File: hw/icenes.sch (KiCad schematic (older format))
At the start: 72 parts, among them J1 USB_B_Micro, J2 Barrel_Jack_Switch, U1 TPS62050, U2 TPS62050, U3 TPS62056, U4 iCE40HX8K-CT256

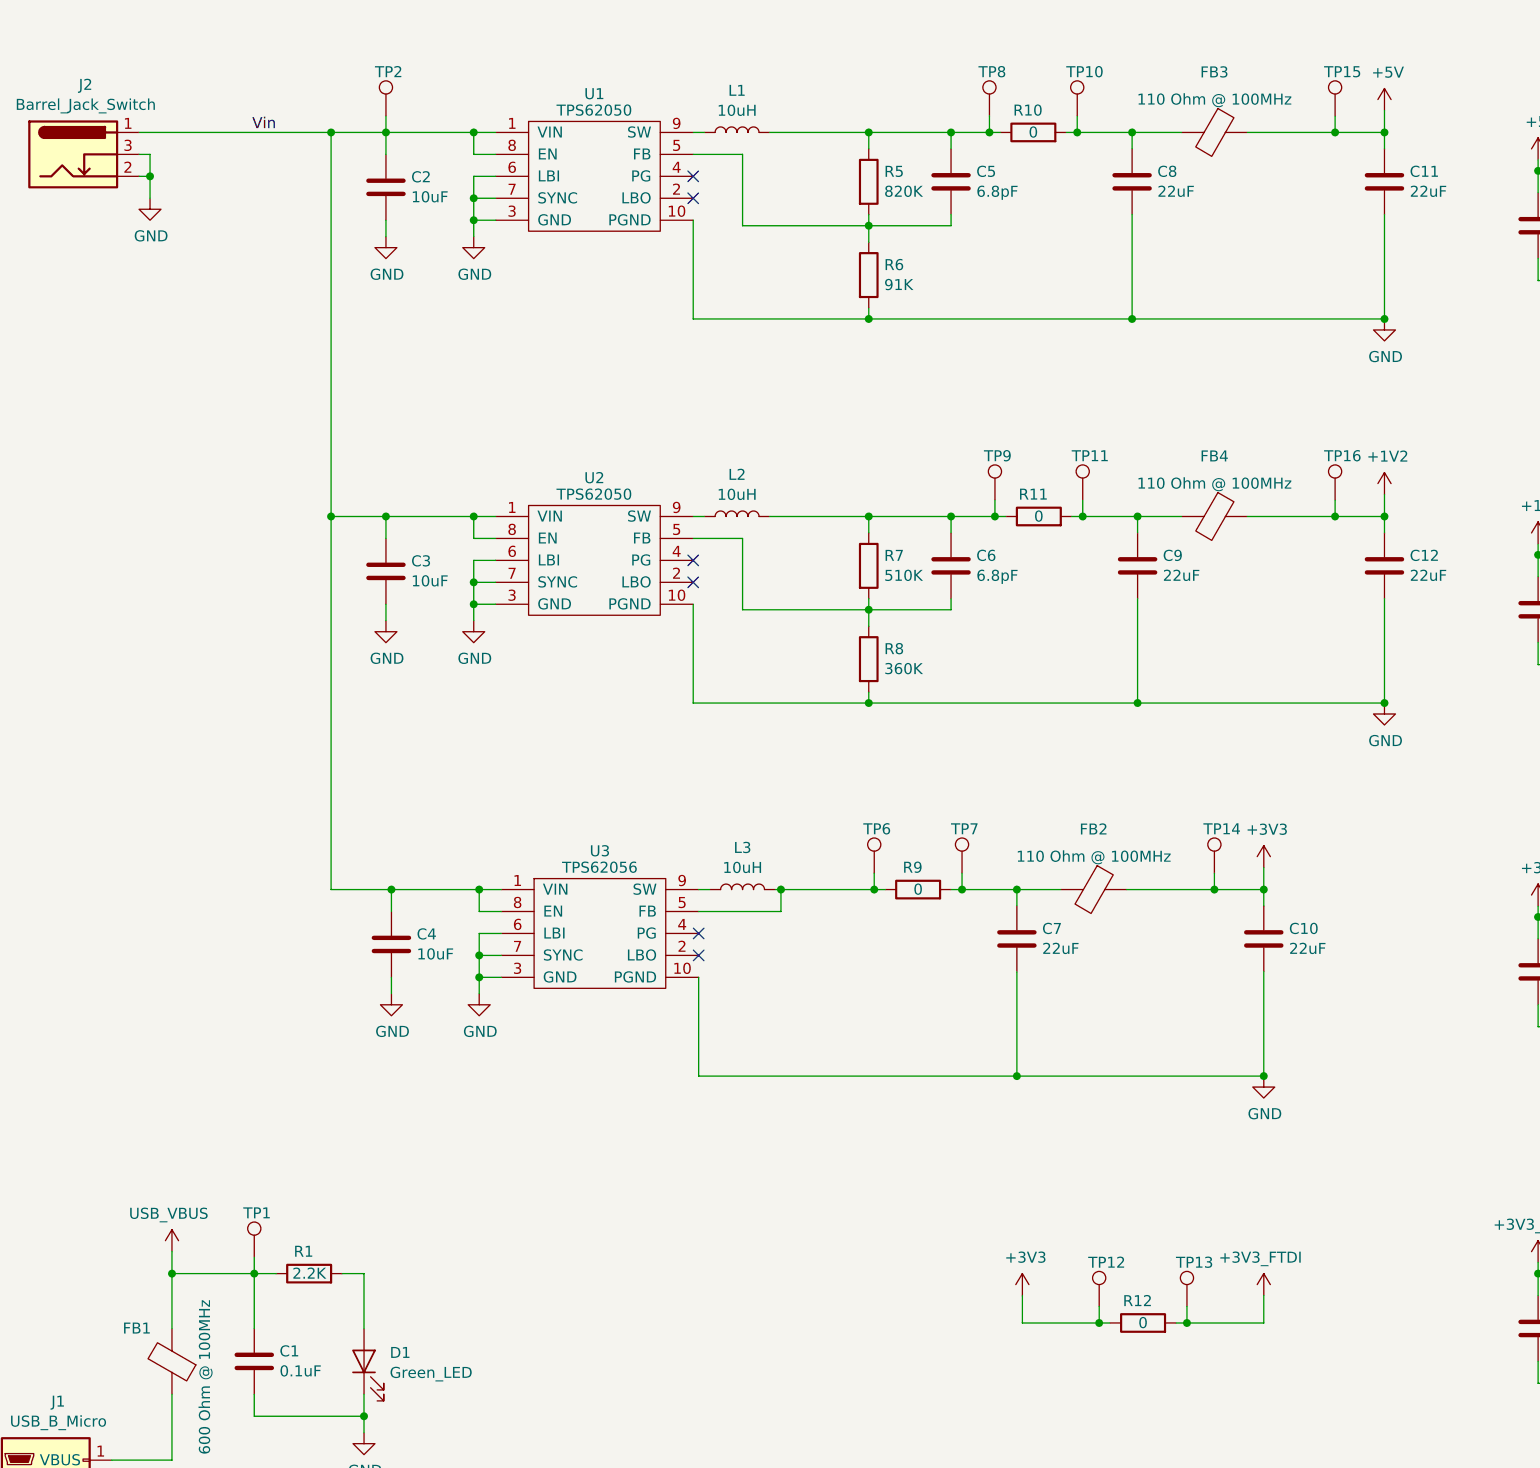
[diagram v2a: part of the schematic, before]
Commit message: Added voltage range in Vin lable (+5V to +10V).
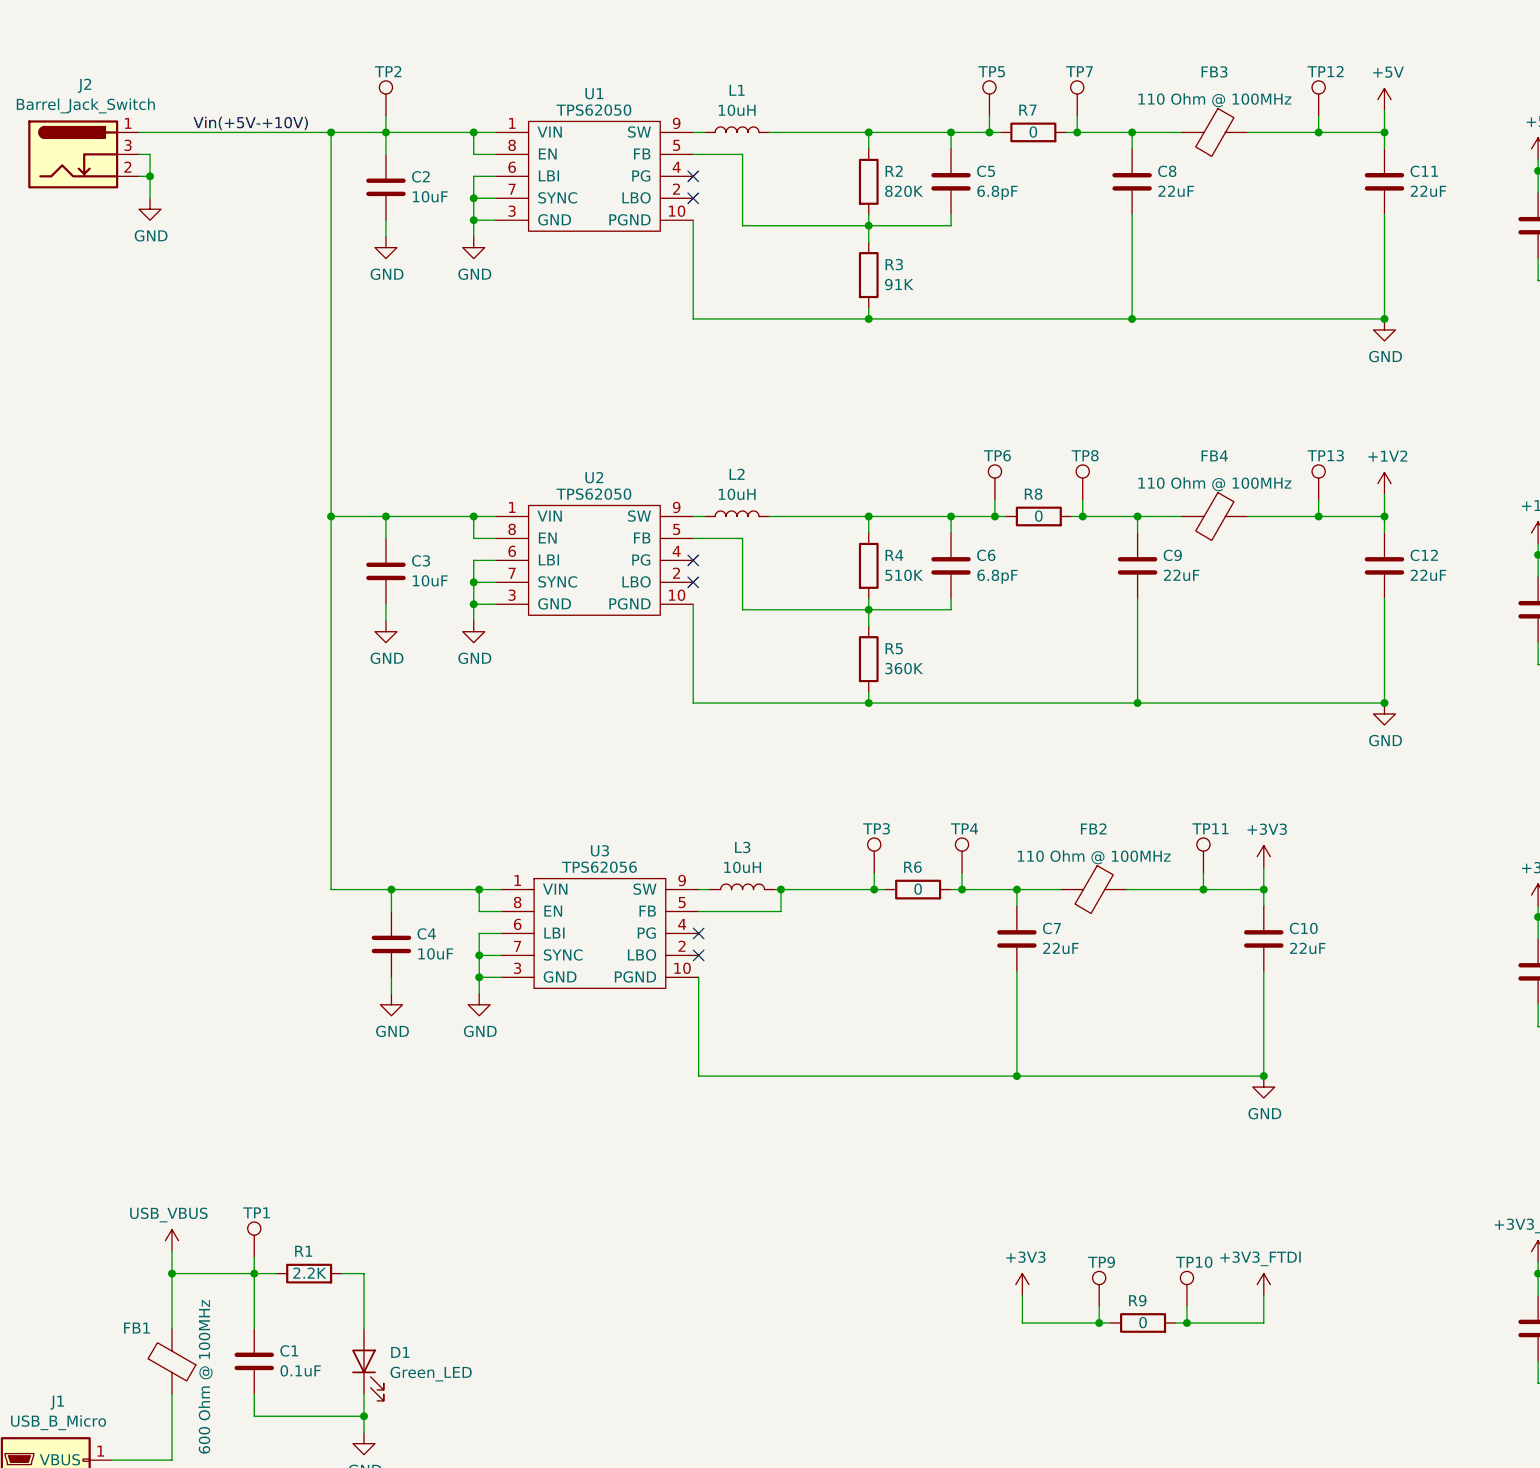
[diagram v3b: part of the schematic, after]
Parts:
- renumbered R5 to R2, R6 to R3, R7 to R4, R8 to R5, R9 to R6, R10 to R7, R11 to R8, R12 to R9, TP13 to TP10, TP14 to TP11, TP15 to TP12, TP16 to TP13, TP6 to TP3, TP7 to TP4, TP8 to TP5, TP9 to TP6, TP10 to TP7, TP11 to TP8, TP12 to TP9
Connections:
- net Vin renamed Vin(+5V-+10V)
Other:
- moved on the sheet: TP11, TP12, TP13
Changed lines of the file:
@@
 F1 "icenes-nes-connector.sch" 50
 $EndSheet
-Text Label 3000 1550 2    50   ~ 0
-Vin
+Text Label 3150 1550 2    50   ~ 0
+Vin(+5V-+10V)
 $Comp
 L power:+3V3 #PWR012
@@
 	6075 5000 6125 5000
 $Comp
-L icenes-library:R0 R9
+L icenes-library:R0 R6
 U 1 1 5D6A7F7F
 P 5925 5000
-F 0 "R9" H 5900 5100 50  0000 C CNN
+F 0 "R6" H 5900 5100 50  0000 C CNN
 F 1 "R0" H 5925 4900 50  0001 C CNN
 F 2 "Resistor_SMD:R_0805_2012Metric_Pad1.15x1.40mm_HandSolder" V 5925 5000 50  0001 C CNN
@@
 	6625 3300 6675 3300
 $Comp
-L icenes-library:R0 R11
+L icenes-library:R0 R8
 U 1 1 5D56A60B
 P 6475 3300
-F 0 "R11" H 6450 3400 50  0000 C CNN
+F 0 "R8" H 6450 3400 50  0000 C CNN
 F 1 "R0" H 6475 3200 50  0001 C CNN
 F 2 "Resistor_SMD:R_0805_2012Metric_Pad1.15x1.40mm_HandSolder" V 6475 3300 50  0001 C CNN
@@
 $EndComp
 $Comp
-L icenes-library:R360K R8
+L icenes-library:R360K R5
 U 1 1 5D43172D
 P 5700 3950
-F 0 "R8" V 5654 4020 50  0000 L CNN
+F 0 "R5" V 5654 4020 50  0000 L CNN
 F 1 "R360K" H 5700 3850 50  0001 C CNN
 F 2 "Resistor_SMD:R_0603_1608Metric_Pad1.05x0.95mm_HandSolder" V 5700 3950 50  0001 C CNN
@@
 $EndComp
 $Comp
-L icenes-library:R510K R7
+L icenes-library:R510K R4
 U 1 1 5D4301E7
 P 5700 3525
-F 0 "R7" V 5654 3595 50  0000 L CNN
+F 0 "R4" V 5654 3595 50  0000 L CNN
 F 1 "R510K" H 5700 3425 50  0001 C CNN
 F 2 "Resistor_SMD:R_0603_1608Metric_Pad1.05x0.95mm_HandSolder" V 5700 3525 50  0001 C CNN
@@
 $EndComp
 $Comp
-L icenes-library:R0 R10
+L icenes-library:R0 R7
 U 1 1 5D4F2DE1
 P 6450 1550
-F 0 "R10" H 6425 1650 50  0000 C CNN
+F 0 "R7" H 6425 1650 50  0000 C CNN
 F 1 "R0" H 6450 1450 50  0001 C CNN
 F 2 "Resistor_SMD:R_0805_2012Metric_Pad1.15x1.40mm_HandSolder" V 6450 1550 50  0001 C CNN
@@
 Connection ~ 6075 1550
 $Comp
-L icenes-library:R820K R5
+L icenes-library:R820K R2
 U 1 1 5D37D2E8
 P 5700 1775
-F 0 "R5" V 5654 1845 50  0000 L CNN
+F 0 "R2" V 5654 1845 50  0000 L CNN
 F 1 "R820K" H 5700 1675 50  0001 C CNN
 F 2 "Resistor_SMD:R_0603_1608Metric_Pad1.05x0.95mm_HandSolder" V 5700 1775 50  0001 C CNN
@@
 $EndComp
 $Comp
-L icenes-library:R91K R6
+L icenes-library:R91K R3
 U 1 1 5D37EA73
 P 5700 2200
-F 0 "R6" V 5654 2270 50  0000 L CNN
+F 0 "R3" V 5654 2270 50  0000 L CNN
 F 1 "R91K" H 5700 2100 50  0001 C CNN
 F 2 "Resistor_SMD:R_0603_1608Metric_Pad1.05x0.95mm_HandSolder" V 5700 2200 50  0001 C CNN
@@
 $EndComp
 $Comp
-L icenes-library:TestPoint TP8
+L icenes-library:TestPoint TP5
 U 1 1 5D7111E6
 P 6250 1475
-F 0 "TP8" H 6200 1675 50  0000 L CNN
+F 0 "TP5" H 6200 1675 50  0000 L CNN
 F 1 "TestPoint" H 6250 1675 50  0001 C CNN
 F 2 "TestPoint:TestPoint_Pad_D1.0mm" H 6450 1475 50  0001 C CNN
@@
 $EndComp
 $Comp
-L icenes-library:TestPoint TP10
+L icenes-library:TestPoint TP7
 U 1 1 5D712B7B
 P 6650 1475
-F 0 "TP10" H 6600 1675 50  0000 L CNN
+F 0 "TP7" H 6600 1675 50  0000 L CNN
 F 1 "TestPoint" H 6650 1675 50  0001 C CNN
 F 2 "TestPoint:TestPoint_Pad_D1.0mm" H 6850 1475 50  0001 C CNN
@@
 $EndComp
 $Comp
-L icenes-library:TestPoint TP9
+L icenes-library:TestPoint TP6
 U 1 1 5D724BBE
 P 6275 3225
-F 0 "TP9" H 6225 3425 50  0000 L CNN
+F 0 "TP6" H 6225 3425 50  0000 L CNN
 F 1 "TestPoint" H 6275 3425 50  0001 C CNN
 F 2 "TestPoint:TestPoint_Pad_D1.0mm" H 6475 3225 50  0001 C CNN
@@
 $EndComp
 $Comp
-L icenes-library:TestPoint TP11
+L icenes-library:TestPoint TP8
 U 1 1 5D735BB7
 P 6675 3225
-F 0 "TP11" H 6625 3425 50  0000 L CNN
+F 0 "TP8" H 6625 3425 50  0000 L CNN
 F 1 "TestPoint" H 6675 3425 50  0001 C CNN
 F 2 "TestPoint:TestPoint_Pad_D1.0mm" H 6875 3225 50  0001 C CNN
@@
 $EndComp
 $Comp
-L icenes-library:TestPoint TP6
+L icenes-library:TestPoint TP3
 U 1 1 5D746D9B
 P 5725 4925
-F 0 "TP6" H 5675 5125 50  0000 L CNN
+F 0 "TP3" H 5675 5125 50  0000 L CNN
 F 1 "TestPoint" H 5725 5125 50  0001 C CNN
 F 2 "TestPoint:TestPoint_Pad_D1.0mm" H 5925 4925 50  0001 C CNN
@@
 $EndComp
 $Comp
-L icenes-library:TestPoint TP7
+L icenes-library:TestPoint TP4
 U 1 1 5D758010
 P 6125 4925
-F 0 "TP7" H 6075 5125 50  0000 L CNN
+F 0 "TP4" H 6075 5125 50  0000 L CNN
 F 1 "TestPoint" H 6125 5125 50  0001 C CNN
 F 2 "TestPoint:TestPoint_Pad_D1.0mm" H 6325 4925 50  0001 C CNN
@@
 Connection ~ 8050 1550
 Connection ~ 8050 2400
-Wire Wire Line
-	7825 1475 7825 1550
-$Comp
-L icenes-library:TestPoint TP15
+$Comp
+L icenes-library:TestPoint TP12
 U 1 1 5D69F2EA
-P 7825 1475
-F 0 "TP15" H 7775 1675 50  0000 L CNN
-F 1 "TestPoint" H 7825 1675 50  0001 C CNN
-F 2 "TestPoint:TestPoint_Pad_D1.0mm" H 8025 1475 50  0001 C CNN
-F 3 "~" H 8025 1475 50  0001 C CNN
-	1    7825 1475
-	1    0    0    -1
-$EndComp
-Connection ~ 7825 1550
+P 7750 1475
+F 0 "TP12" H 7700 1675 50  0000 L CNN
+F 1 "TestPoint" H 7750 1675 50  0001 C CNN
+F 2 "TestPoint:TestPoint_Pad_D1.0mm" H 7950 1475 50  0001 C CNN
+F 3 "~" H 7950 1475 50  0001 C CNN
+	1    7750 1475
+	1    0    0    -1
+$EndComp
 Wire Wire Line
 	6900 2400 8050 2400
@@
 	8050 3300 8050 3375
 Connection ~ 8050 3300
-Wire Wire Line
-	7825 3225 7825 3300
-$Comp
-L icenes-library:TestPoint TP16
+$Comp
+L icenes-library:TestPoint TP13
 U 1 1 5D7086C1
-P 7825 3225
-F 0 "TP16" H 7775 3425 50  0000 L CNN
-F 1 "TestPoint" H 7825 3425 50  0001 C CNN
-F 2 "TestPoint:TestPoint_Pad_D1.0mm" H 8025 3225 50  0001 C CNN
-F 3 "~" H 8025 3225 50  0001 C CNN
-	1    7825 3225
-	1    0    0    -1
-$EndComp
-Connection ~ 7825 3300
+P 7750 3225
+F 0 "TP13" H 7700 3425 50  0000 L CNN
+F 1 "TestPoint" H 7750 3425 50  0001 C CNN
+F 2 "TestPoint:TestPoint_Pad_D1.0mm" H 7950 3225 50  0001 C CNN
+F 3 "~" H 7950 3225 50  0001 C CNN
+	1    7750 3225
+	1    0    0    -1
+$EndComp
 Wire Wire Line
 	5700 4150 6925 4150
@@
 	7500 5000 7500 5075
 Connection ~ 7500 5000
-Wire Wire Line
-	7275 4925 7275 5000
-$Comp
-L icenes-library:TestPoint TP14
+$Comp
+L icenes-library:TestPoint TP11
 U 1 1 5D7AD8D4
-P 7275 4925
-F 0 "TP14" H 7225 5125 50  0000 L CNN
-F 1 "TestPoint" H 7275 5125 50  0001 C CNN
-F 2 "TestPoint:TestPoint_Pad_D1.0mm" H 7475 4925 50  0001 C CNN
-F 3 "~" H 7475 4925 50  0001 C CNN
-	1    7275 4925
-	1    0    0    -1
-$EndComp
-Connection ~ 7275 5000
+P 7225 4925
+F 0 "TP11" H 7175 5125 50  0000 L CNN
+F 1 "TestPoint" H 7225 5125 50  0001 C CNN
+F 2 "TestPoint:TestPoint_Pad_D1.0mm" H 7425 4925 50  0001 C CNN
+F 3 "~" H 7425 4925 50  0001 C CNN
+	1    7225 4925
+	1    0    0    -1
+$EndComp
 Wire Wire Line
 	6375 5850 7500 5850
 Connection ~ 7500 5850
 Wire Wire Line
-	7425 1550 7825 1550
-Wire Wire Line
 	7125 1550 6900 1550
 Connection ~ 6900 1550
 Wire Wire Line
-	7425 3300 7825 3300
-Wire Wire Line
 	7125 3300 6925 3300
 Connection ~ 6925 3300
-Wire Wire Line
-	6875 5000 7275 5000
 Wire Wire Line
 	6575 5000 6375 5000
@@
 Wire Wire Line
 	14300 7250 14100 7250
-Wire Wire Line
-	7275 5000 7500 5000
-Wire Wire Line
-	7825 3300 8050 3300
-Wire Wire Line
-	7825 1550 8050 1550
 $Comp
 L power:GND #PWR024
@@
 	7100 6975 7150 6975
 $Comp
-L icenes-library:R0 R12
+L icenes-library:R0 R9
 U 1 1 5DBD6898
 P 6950 6975
-AR Path="/5DBD6898" Ref="R12"  Part="1"
+AR Path="/5DBD6898" Ref="R9"  Part="1"
 AR Path="/5D1BAC88/5DBD6898" Ref="R?"  Part="1"
-F 0 "R12" H 6925 7075 50  0000 C CNN
+F 0 "R9" H 6925 7075 50  0000 C CNN
 F 1 "R0" H 6950 6875 50  0001 C CNN
 F 2 "Resistor_SMD:R_0805_2012Metric_Pad1.15x1.40mm_HandSolder" V 6950 6975 50  0001 C CNN
@@
 	6400 6975 6750 6975
 $Comp
-L icenes-library:TestPoint TP12
+L icenes-library:TestPoint TP9
 U 1 1 5DBD68AA
 P 6750 6900
-AR Path="/5DBD68AA" Ref="TP12"  Part="1"
+AR Path="/5DBD68AA" Ref="TP9"  Part="1"
 AR Path="/5D1BAC88/5DBD68AA" Ref="TP?"  Part="1"
-F 0 "TP12" H 6700 7100 50  0000 L CNN
+F 0 "TP9" H 6700 7100 50  0000 L CNN
 F 1 "TestPoint" H 6750 7100 50  0001 C CNN
 F 2 "TestPoint:TestPoint_Pad_D1.0mm" H 6950 6900 50  0001 C CNN
@@
 $EndComp
 $Comp
-L icenes-library:TestPoint TP13
+L icenes-library:TestPoint TP10
 U 1 1 5DBD68B0
 P 7150 6900
-AR Path="/5DBD68B0" Ref="TP13"  Part="1"
+AR Path="/5DBD68B0" Ref="TP10"  Part="1"
 AR Path="/5D1BAC88/5DBD68B0" Ref="TP?"  Part="1"
-F 0 "TP13" H 7100 7100 50  0000 L CNN
+F 0 "TP10" H 7100 7100 50  0000 L CNN
 F 1 "TestPoint" H 7150 7100 50  0001 C CNN
 F 2 "TestPoint:TestPoint_Pad_D1.0mm" H 7350 6900 50  0001 C CNN
@@
 	5300 5000 5725 5000
 NoConn ~ 4925 5200
+Wire Wire Line
+	7425 1550 7750 1550
+Wire Wire Line
+	7750 1475 7750 1550
+Connection ~ 7750 1550
+Wire Wire Line
+	7750 1550 8050 1550
+Wire Wire Line
+	7425 3300 7750 3300
+Wire Wire Line
+	7750 3225 7750 3300
+Connection ~ 7750 3300
+Wire Wire Line
+	7750 3300 8050 3300
+Wire Wire Line
+	6875 5000 7225 5000
+Wire Wire Line
+	7225 4925 7225 5000
+Connection ~ 7225 5000
+Wire Wire Line
+	7225 5000 7500 5000
 $EndSCHEMATC

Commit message: Changed inductor.
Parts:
- L1, L2, L3: footprint Inductor_SMD:L_1812_4532Metric_Pad1.30x3.40mm_HandSolder -> icenes-library:Sumida_L_7.5x7.5_H4.5; Manufacturer Coilcraft -> Sumida; Part number 1812PS-103JLB -> CDRH74NP-100MC-B
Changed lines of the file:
@@
 F 0 "L3" V 5315 5000 50  0000 C CNN
 F 1 "L10uH" V 5200 5000 50  0001 C CNN
-F 2 "Inductor_SMD:L_1812_4532Metric_Pad1.30x3.40mm_HandSolder" H 5125 5000 50  0001 C CNN
-F 3 "https://www.mouser.se/datasheet/2/597/1812ps-270619.pdf" H 5125 5000 50  0001 C CNN
+F 2 "icenes-library:Sumida_L_7.5x7.5_H4.5" H 5125 5000 50  0001 C CNN
+F 3 "https://www.mouser.se/datasheet/2/390/CDRH74-514269.pdf" H 5125 5000 50  0001 C CNN
 F 4 "10uH" V 5224 5000 50  0000 C CNN "Inductance"
-F 5 "Coilcraft " H 5125 5000 50  0001 C CNN "Manufacturer"
-F 6 "1812PS-103JLB" H 5125 5000 50  0001 C CNN "Part number"
+F 5 "Sumida " H 5125 5000 50  0001 C CNN "Manufacturer"
+F 6 "CDRH74NP-100MC-B" H 5125 5000 50  0001 C CNN "Part number"
 	1    5125 5000
 	0    -1   -1   0
@@
 F 0 "L2" V 5290 3300 50  0000 C CNN
 F 1 "L10uH" V 5175 3300 50  0001 C CNN
-F 2 "Inductor_SMD:L_1812_4532Metric_Pad1.30x3.40mm_HandSolder" H 5100 3300 50  0001 C CNN
-F 3 "https://www.mouser.se/datasheet/2/597/1812ps-270619.pdf" H 5100 3300 50  0001 C CNN
+F 2 "icenes-library:Sumida_L_7.5x7.5_H4.5" H 5100 3300 50  0001 C CNN
+F 3 "https://www.mouser.se/datasheet/2/390/CDRH74-514269.pdf" H 5100 3300 50  0001 C CNN
 F 4 "10uH" V 5199 3300 50  0000 C CNN "Inductance"
-F 5 "Coilcraft " H 5100 3300 50  0001 C CNN "Manufacturer"
-F 6 "1812PS-103JLB" H 5100 3300 50  0001 C CNN "Part number"
+F 5 "Sumida " H 5100 3300 50  0001 C CNN "Manufacturer"
+F 6 "CDRH74NP-100MC-B" H 5100 3300 50  0001 C CNN "Part number"
 	1    5100 3300
 	0    -1   -1   0
@@
 F 0 "L1" V 5290 1550 50  0000 C CNN
 F 1 "L10uH" V 5175 1550 50  0001 C CNN
-F 2 "Inductor_SMD:L_1812_4532Metric_Pad1.30x3.40mm_HandSolder" H 5100 1550 50  0001 C CNN
-F 3 "https://www.mouser.se/datasheet/2/597/1812ps-270619.pdf" H 5100 1550 50  0001 C CNN
+F 2 "icenes-library:Sumida_L_7.5x7.5_H4.5" H 5100 1550 50  0001 C CNN
+F 3 "https://www.mouser.se/datasheet/2/390/CDRH74-514269.pdf" H 5100 1550 50  0001 C CNN
 F 4 "10uH" V 5199 1550 50  0000 C CNN "Inductance"
-F 5 "Coilcraft " H 5100 1550 50  0001 C CNN "Manufacturer"
-F 6 "1812PS-103JLB" H 5100 1550 50  0001 C CNN "Part number"
+F 5 "Sumida " H 5100 1550 50  0001 C CNN "Manufacturer"
+F 6 "CDRH74NP-100MC-B" H 5100 1550 50  0001 C CNN "Part number"
 	1    5100 1550
 	0    -1   -1   0

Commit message: Fixed incorrect reference between USB_VBUS and +3V3_FTDI
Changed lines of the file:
@@
-	1    0    0    -1
-$EndComp
-$Comp
-L icenes-library:USB_VBUS #PWR03
-U 1 1 5D967EB3
-P 2525 6500
-F 0 "#PWR03" H 2525 6500 50  0001 C CNN
-F 1 "USB_VBUS" H 2510 6523 50  0000 C CNN
-F 2 "" H 2525 6500 50  0001 C CNN
-F 3 "" H 2525 6500 50  0001 C CNN
-	1    2525 6500
 	1    0    0    -1
 $EndComp
@@
 Wire Wire Line
 	13750 1250 13750 1300
-Wire Wire Line
-	14250 1250 14250 1300
 NoConn ~ 4900 1850
 NoConn ~ 4900 3600
@@
 Wire Wire Line
 	7225 5000 7500 5000
+Wire Wire Line
+	14250 1250 14250 1300
+$Comp
+L icenes-library:USB_VBUS #PWR03
+U 1 1 5D967EB3
+P 2525 6500
+F 0 "#PWR03" H 2525 6500 50  0001 C CNN
+F 1 "USB_VBUS" H 2510 6523 50  0000 C CNN
+F 2 "" H 2525 6500 50  0001 C CNN
+F 3 "" H 2525 6500 50  0001 C CNN
+	1    2525 6500
+	1    0    0    -1
+$EndComp
+$Comp
+L icenes-library:USB_VBUS #PWR0160
+U 1 1 5D99F6A0
+P 14750 1100
+F 0 "#PWR0160" H 14750 1100 50  0001 C CNN
+F 1 "USB_VBUS" H 14735 1123 50  0000 C CNN
+F 2 "" H 14750 1100 50  0001 C CNN
+F 3 "" H 14750 1100 50  0001 C CNN
+	1    14750 1100
+	1    0    0    -1
+$EndComp
+$Comp
+L power:PWR_FLAG #FLG0101
+U 1 1 5D9B9803
+P 14750 1300
+F 0 "#FLG0101" H 14750 1375 50  0001 C CNN
+F 1 "PWR_FLAG" H 14750 1473 50  0000 C CNN
+F 2 "" H 14750 1300 50  0001 C CNN
+F 3 "~" H 14750 1300 50  0001 C CNN
+	1    14750 1300
+	-1   0    0    1
+$EndComp
+Wire Wire Line
+	14750 1250 14750 1300
 $EndSCHEMATC

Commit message: Layout.
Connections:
- net USB_DM renamed USB_D_N
- net USB_DP renamed USB_D_P
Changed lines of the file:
@@
 $EndComp
 Text GLabel 2325 7900 2    50   BiDi ~ 0
-USB_DM
+USB_D_N
 Text GLabel 2325 7800 2    50   BiDi ~ 0
-USB_DP
+USB_D_P
 Wire Wire Line
 	2250 7800 2325 7800
